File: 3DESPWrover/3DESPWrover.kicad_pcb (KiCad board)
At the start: 2 copper layers, 40 x 40 mm, 21 parts, among them J1 Conn_01x05_Male, J2 Conn_01x04, J3 Conn_02x03_Odd_Even, J4 Conn_02x07_Odd_Even, SW1 SW_Push, SW2 SW_Push, U1 ESP32-S2-WROVER

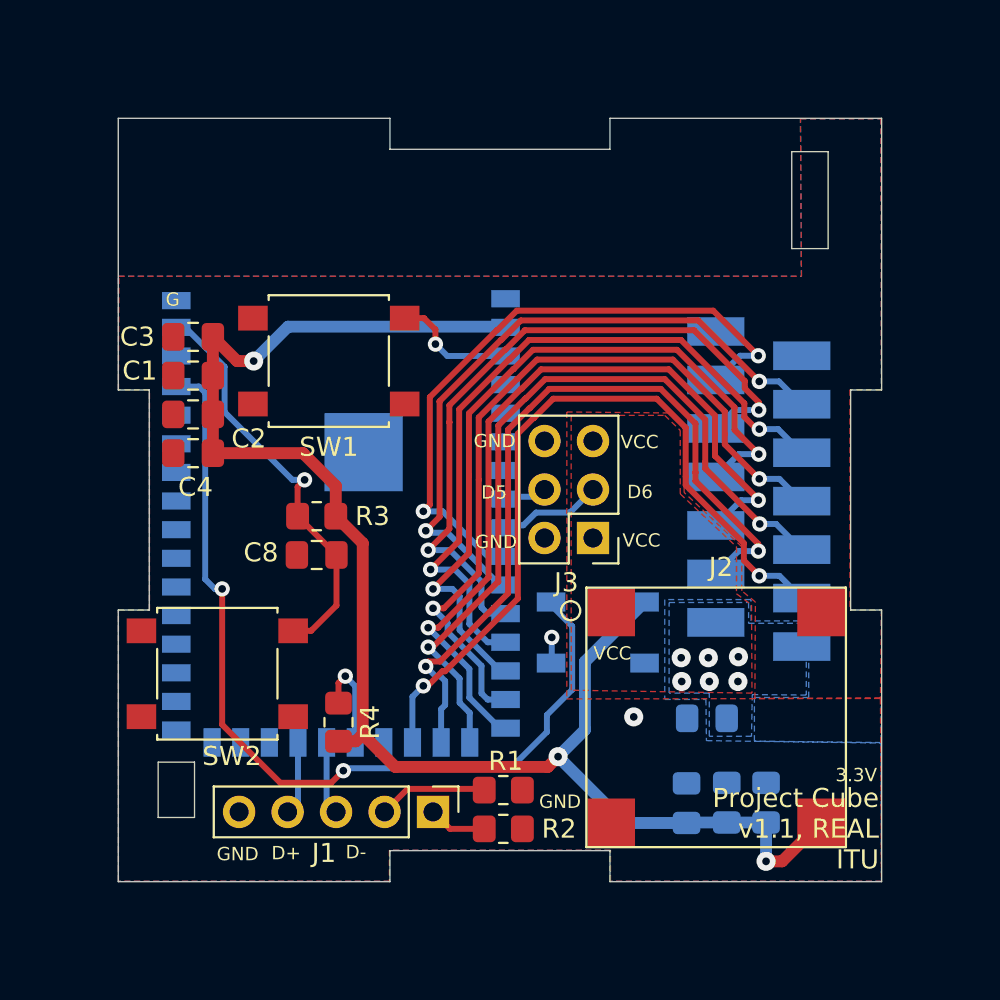
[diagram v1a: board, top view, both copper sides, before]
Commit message: Corrected switching step down power source connections and added mill corner paths
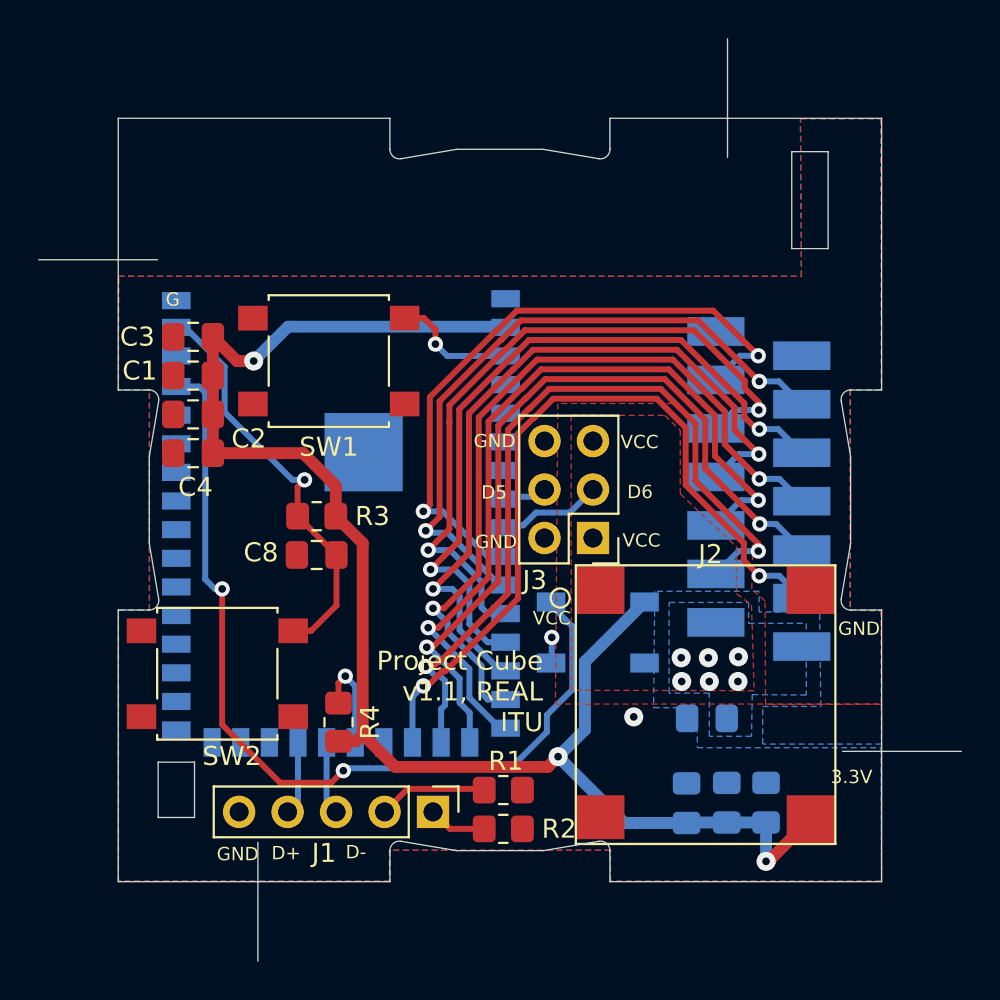
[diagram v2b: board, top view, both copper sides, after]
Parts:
- moved J2 0.87 mm to (230.7, 80.7)
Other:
- board size 40 x 40 mm -> 48.3 x 48.3 mm

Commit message: Ordered
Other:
- net class Default removed
- net class Power removed

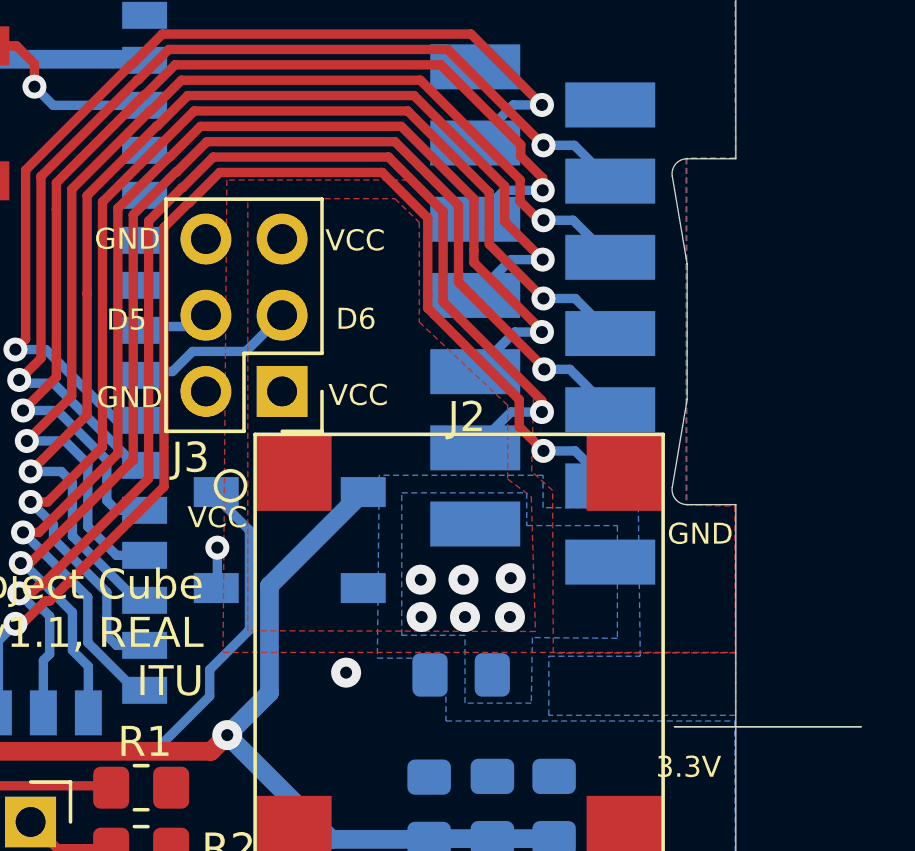
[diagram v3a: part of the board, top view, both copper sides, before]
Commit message: Added 0805 diode before 3.3 power source
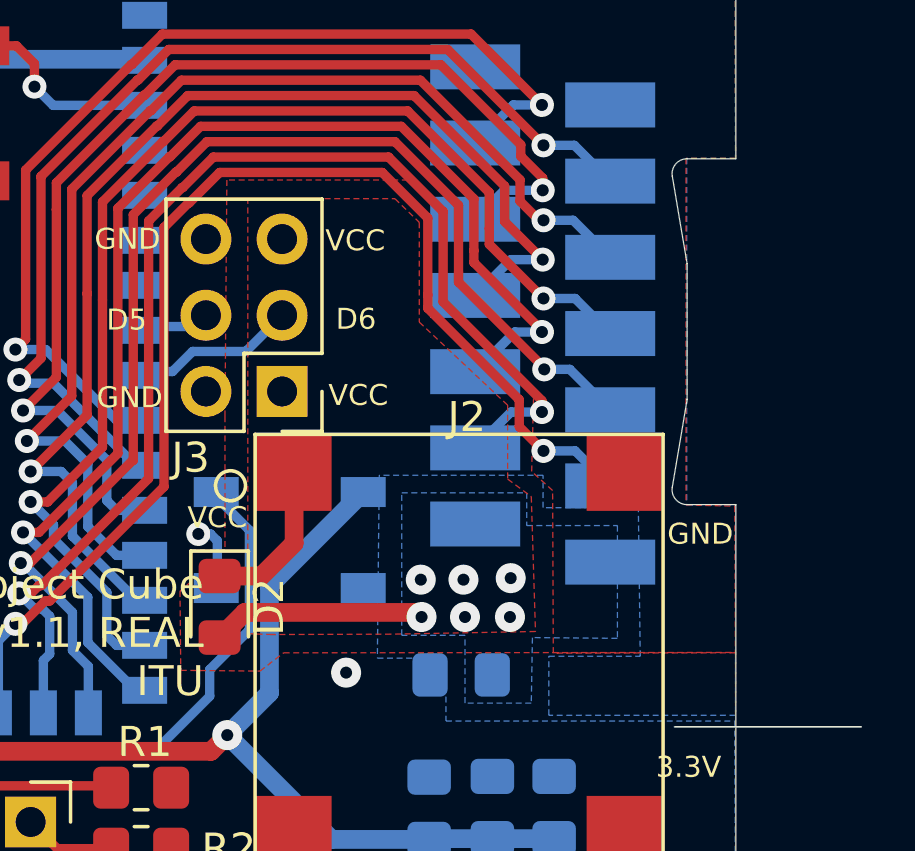
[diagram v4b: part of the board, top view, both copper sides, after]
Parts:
- added D2: D, Diode_SMD:D_0805_2012Metric_Pad1.15x1.40mm_HandSolder, F.Cu at (222.7, 79.2)
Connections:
- D1 pad 2: Net-(D1-Pad2) -> unconnected-(D1-Pad2)
- J2 pad 1: /Vin -> Net-(J2-Pad1)
- J2 pad 4: Net-(J2-Pad4) -> unconnected-(J2-Pad4)
- U1 pad 40: Net-(U1-Pad40) -> unconnected-(U1-Pad40)
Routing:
- net /Vin: track 0.00 -> 7.14 mm
- net Net-(J2-Pad1): track 0.00 -> 6.21 mm
- net GND: track 1.62 -> 2.57 mm
